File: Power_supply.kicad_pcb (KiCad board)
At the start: 2 copper layers, 160 x 40 mm, 49 parts, among them J20 HV_Transformer, J21 LV_Transformer, J22 220V, J23 Transformers, J24 Thyratrone, J25 Anodes_enable, J26 Conn_01x04, J27 Conn_01x04, J28 Conn_01x04, K2 SANYOU_SRD_Form_C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

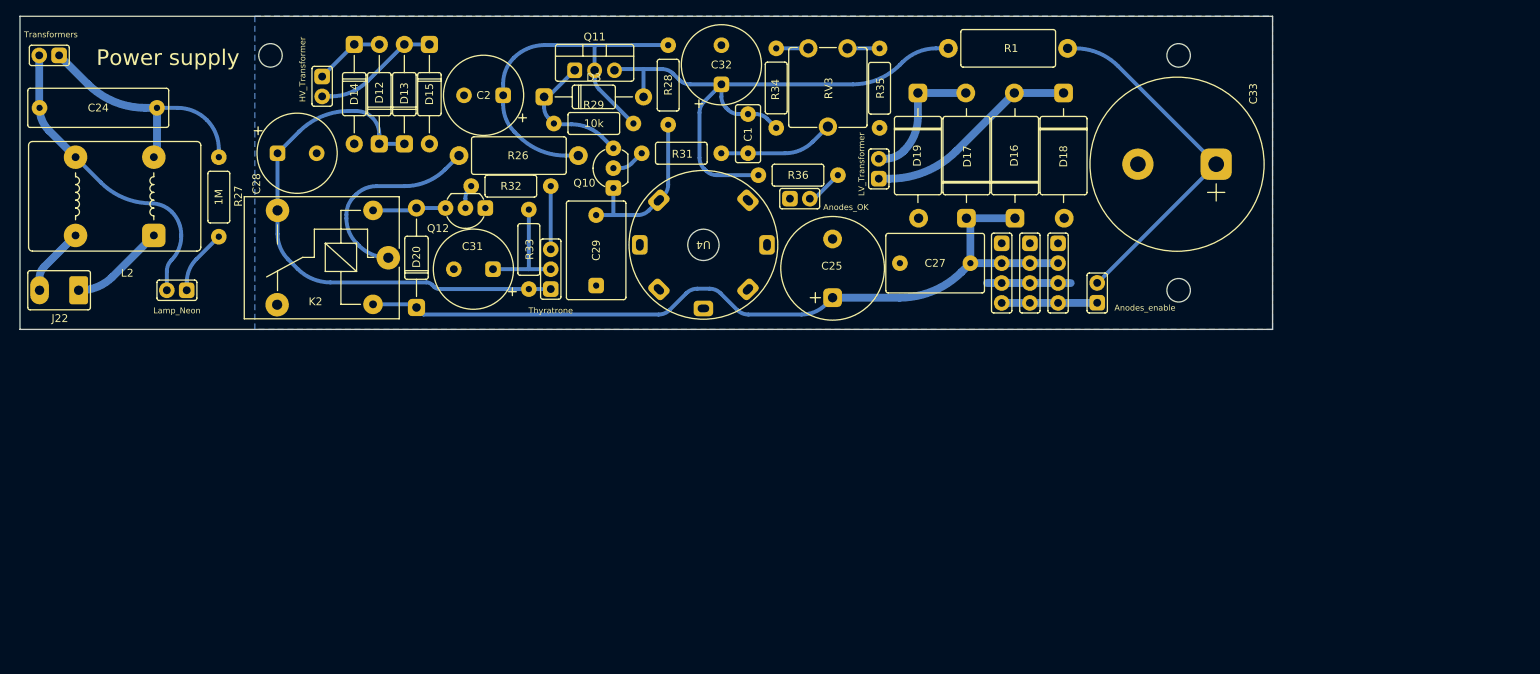
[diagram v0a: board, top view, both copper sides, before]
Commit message: New power supply PCB
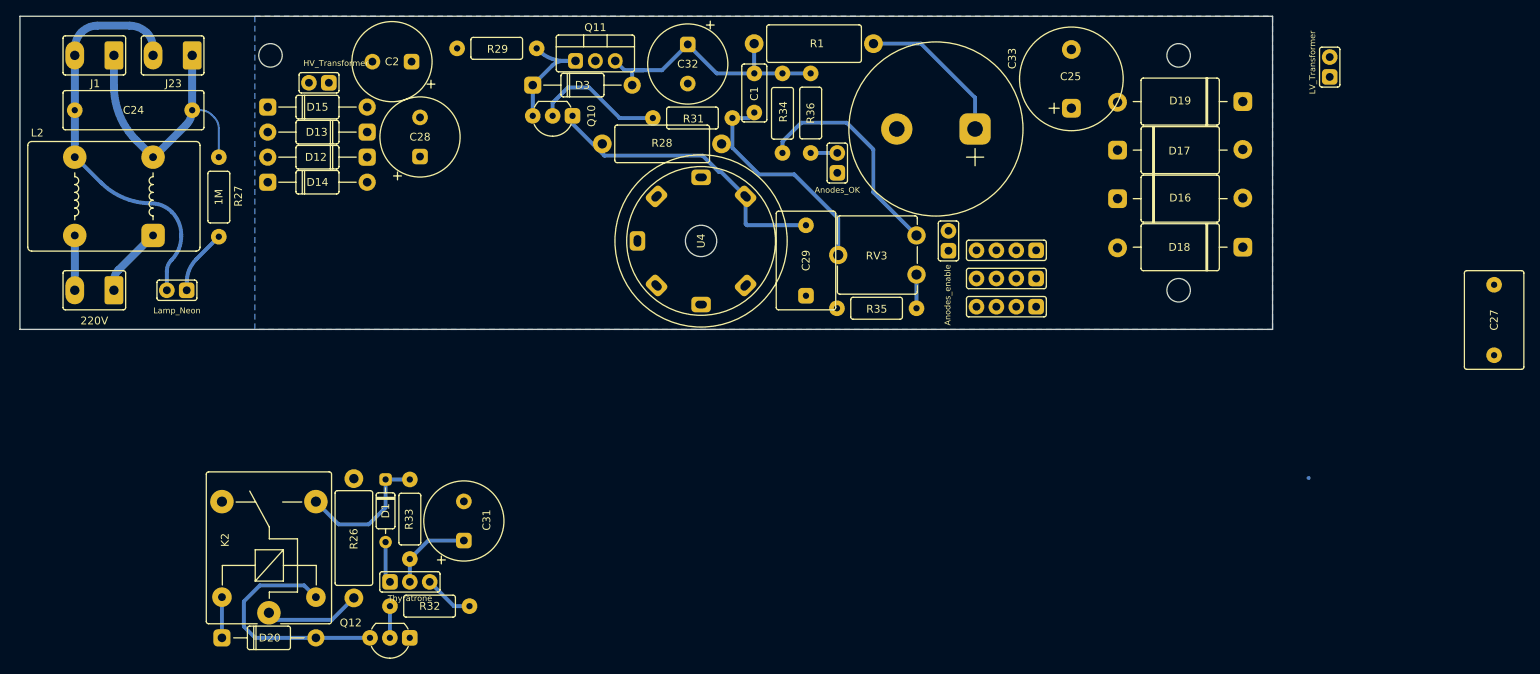
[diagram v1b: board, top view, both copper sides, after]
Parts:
- added D1: BZX55C75, spdf1626_lib:D_THT_DO-35_SOD27_Horizontal, F.Cu at (76.7, 153.2)
- added J1: Transformers, spdf1626_lib:Connector_1x02_P5mm_Vertical, F.Cu at (39.5, 95.0)
- J23: footprint spdf1626_lib:PinHeader_1x02_P2.54mm -> spdf1626_lib:Connector_1x02_P5mm_Vertical
- K2: footprint Relay_THT:Relay_SPDT_SANYOU_SRD_Series_Form_C -> spdf1626_lib:Relay_THT_SRD_Series
- R28: footprint spdf1626_lib:R_THT_025W -> spdf1626_lib:R_THT_1W
- moved C27 71.8 mm to (218.3, 128.8), turned to 90 degrees
- moved J21 59.0 mm to (197.3, 97.7)
- moved R26 58.1 mm to (72.7, 164.3), turned to 90 degrees
- moved Q12 55.7 mm to (77.2, 169.4)
- moved R32 54.6 mm to (87.4, 165.3)
- moved K2 47.8 mm to (61.8, 166.2), turned to 90 degrees
- moved R33 47.2 mm to (79.8, 159.3), turned to 90 degrees
- moved D20 46.2 mm to (61.8, 169.4), turned to 0 degrees
- moved J24 42.7 mm to (77.3, 162.2), turned to 90 degrees
- moved C25 38.9 mm to (164.3, 101.8)
- moved C31 34.9 mm to (86.7, 157.0), turned to 90 degrees
- moved D19 34.2 mm to (178.2, 100.9), turned to 180 degrees
- moved R35 33.5 mm to (144.5, 127.3), turned to 180 degrees
- moved C33 31.1 mm to (152.0, 104.4)
- moved RV3 27.6 mm to (144.5, 118.0), turned to 180 degrees
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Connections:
- J24 pad 1: HV -> Net-(J24-Pad1)
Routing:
- net +6V: track 104.5 -> 5.20 mm
- net Net-(C2-Pad1): track 55.2 -> 0.00 mm
- net HV: track 69.4 -> 17.7 mm
- net Net-(C1-Pad2): track 77.7 -> 35.5 mm
- net Net-(D16-Pad2): track 27.6 -> 0.00 mm
- net Net-(C33-Pad1): track 46.2 -> 19.9 mm
- net Net-(R34-Pad2): track 4.10 -> 28.7 mm
- net Net-(D20-Pad2): track 9.38 -> 30.6 mm
- net Net-(D17-Pad2): track 17.4 -> 0.00 mm
- net Net-(D13-Pad2): track 16.1 -> 0.00 mm
- net Net-(Q10-Pad1): track 22.2 -> 38.3 mm
- net Net-(C1-Pad1): track 14.8 -> 28.8 mm
- net K1.1: track 26.1 -> 12.4 mm
- net Net-(C24-Pad1): track 40.1 -> 53.4 mm
- net Net-(Q10-Pad2): track 4.31 -> 16.9 mm
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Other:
- board text removed: "Power supply"

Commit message: Working on power supply PCB
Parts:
- moved Q12 53.0 mm to (80.0, 116.5)
- moved J24 50.8 mm to (88.4, 112.7), turned to 0 degrees
- moved R33 50.4 mm to (87.7, 109.5), turned to 180 degrees
- moved R26 50.0 mm to (103.2, 124.7)
- moved R32 44.7 mm to (87.8, 120.7)
- moved D20 44.1 mm to (68.1, 125.8)
- moved K2 44.1 mm to (68.1, 122.6)
- moved C31 42.0 mm to (95.0, 115.8), turned to -90 degrees
- moved D1 40.8 mm to (81.5, 112.7), turned to 0 degrees
- moved C2 17.7 mm to (95.0, 105.3), turned to -90 degrees
- moved R29 12.6 mm to (108.4, 92.0)
- moved D15 10.7 mm to (68.0, 93.0)
- moved D13 10.7 mm to (80.8, 96.2)
- moved D12 10.7 mm to (80.8, 99.4)
- moved D14 10.7 mm to (68.0, 102.6)
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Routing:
- net +6V: track 5.20 -> 75.0 mm
- net K1.1: track 12.4 -> 36.0 mm
- net HV: track 17.7 -> 28.3 mm
- net Net-(C31-Pad1): track 10.8 -> 15.6 mm
- net Net-(J24-Pad3): track 6.36 -> 3.17 mm
- net Net-(J24-Pad1): track 5.33 -> 2.90 mm
- net Net-(Q12-Pad2): track 4.05 -> 5.18 mm
- net Net-(D20-Pad2): track 30.6 -> 30.0 mm

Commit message: Working on power supply PCB
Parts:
- moved R28 30.5 mm to (133.5, 97.2), turned to -90 degrees
- moved R29 20.2 mm to (89.0, 97.6), turned to 0 degrees
- moved Q10 18.7 mm to (116.7, 100.9), turned to 90 degrees
- moved R33 13.6 mm to (85.8, 123.0), turned to 90 degrees
- moved R1 11.3 mm to (112.6, 95.0)
- moved C32 9.79 mm to (109.4, 101.4)
- moved D20 9.27 mm to (61.8, 119.0), turned to 90 degrees
- moved Q11 8.00 mm to (99.2, 102.5)
- moved R31 6.56 mm to (123.7, 109.0), turned to 90 degrees
- moved D1 6.28 mm to (87.3, 110.3)
- moved C2 4.49 mm to (99.2, 106.9)
- moved K2 4.16 mm to (71.5, 125.0)
- moved J24 3.98 mm to (91.8, 114.8)
- moved D3 3.97 mm to (96.7, 95.0)
- moved C31 3.81 mm to (98.5, 117.3)
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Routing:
- net Net-(Q10-Pad1): track 38.3 -> 0.00 mm
- net Net-(R34-Pad2): track 28.7 -> 0.00 mm
- net Net-(D3-Pad1): track 16.0 -> 42.8 mm
- net Net-(C1-Pad1): track 28.8 -> 6.45 mm
- net Net-(C1-Pad2): track 35.5 -> 17.7 mm
- net Net-(C2-Pad1): track 0.00 -> 17.7 mm
- net Net-(D13-Pad2): track 0.00 -> 10.2 mm
- net Net-(Q10-Pad2): track 16.9 -> 7.86 mm
- net Net-(D20-Pad2): track 30.0 -> 25.0 mm
- net Net-(Q12-Pad2): track 5.18 -> 10.1 mm
- net HV: track 28.3 -> 31.1 mm
- net Net-(J24-Pad1): track 2.90 -> 4.67 mm
- net K1.1: track 36.0 -> 34.3 mm
- net Net-(J24-Pad3): track 3.17 -> 4.43 mm
- net Net-(C31-Pad1): track 15.6 -> 16.9 mm

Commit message: New power supply PCB!
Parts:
- moved C27 53.4 mm to (165.0, 125.4), turned to 180 degrees
- moved R29 39.6 mm to (125.8, 112.3), turned to 90 degrees
- moved R28 39.4 mm to (94.9, 104.9), turned to 0 degrees
- moved R35 38.8 mm to (165.8, 94.8), turned to -90 degrees
- moved R1 34.3 mm to (146.9, 94.8), turned to -90 degrees
- moved J21 29.2 mm to (185.8, 124.6), turned to -90 degrees
- moved D3 20.7 mm to (113.9, 106.4), turned to 90 degrees
- moved Q11 20.2 mm to (119.2, 99.5), turned to 90 degrees
- moved NE4 19.8 mm to (153.5, 104.7), turned to -90 degrees
- moved RV3 19.4 mm to (151.1, 99.8), turned to 0 degrees
- moved C32 18.7 mm to (127.9, 98.7), turned to 90 degrees
- moved C31 18.6 mm to (96.5, 98.8), turned to 90 degrees
- moved C33 17.5 mm to (142.1, 118.8)
- moved R32 16.1 mm to (81.1, 108.8), turned to -90 degrees
- moved C25 14.4 mm to (161.6, 115.9)
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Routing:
- net +6V: track 75.0 -> 143.5 mm
- net Net-(C1-Pad1): track 6.45 -> 46.6 mm
- net Net-(C2-Pad1): track 17.7 -> 51.4 mm
- net Net-(D17-Pad2): track 0.00 -> 26.1 mm
- net Net-(C29-Pad2): track 0.00 -> 24.6 mm
- net Net-(C1-Pad2): track 17.7 -> 40.3 mm
- net Net-(D3-Pad1): track 42.8 -> 21.1 mm
- net Net-(NE4-Pad2): track 3.40 -> 17.6 mm
- net 240V: track 0.00 -> 13.7 mm
- net Net-(D16-Pad2): track 0.00 -> 11.6 mm
- net Net-(R34-Pad2): track 0.00 -> 11.5 mm
- net Net-(R35-Pad1): track 4.30 -> 14.7 mm
- net K1.1: track 34.3 -> 24.3 mm
- net GND: track 0.00 -> 8.86 mm
- net HV: track 31.1 -> 38.9 mm
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
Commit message: Power supply PCB final 1.0
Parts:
- turned U4 to 0 degrees
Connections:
- U4 pad 1: Net-(C29-Pad2) -> unconnected-(U4-Pad1)
- U4 pad 4: unconnected-(U4-Pad4) -> GND
- U4 pad 5: unconnected-(U4-Pad5) -> Net-(C29-Pad2)
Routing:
- net Net-(C29-Pad2): track 24.6 -> 35.1 mm
- net +6V: track 143.5 -> 140.5 mm
- net Net-(C1-Pad1): track 46.6 -> 45.4 mm

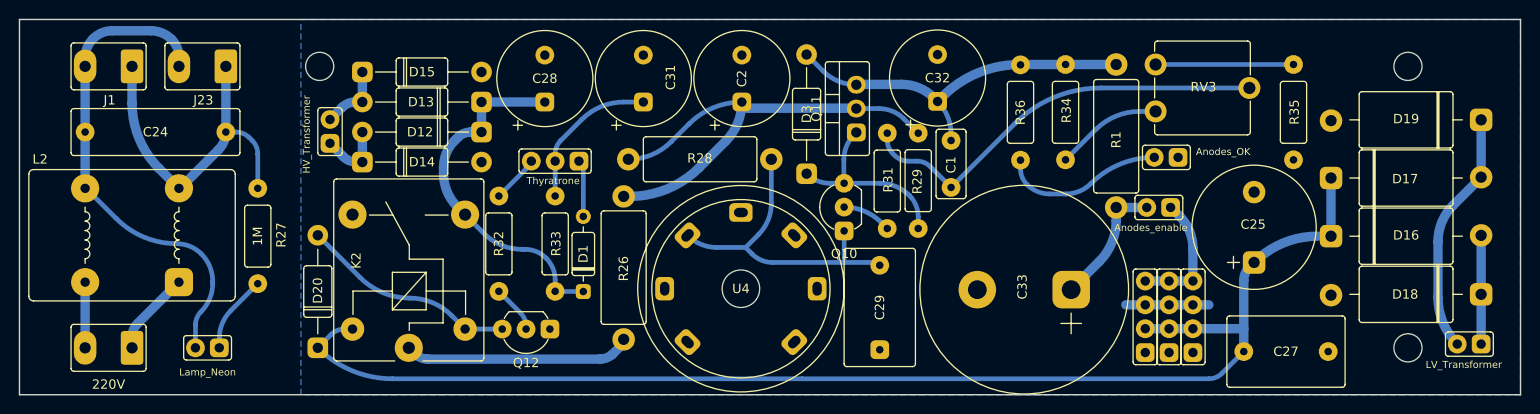
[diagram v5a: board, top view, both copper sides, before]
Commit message: Some errors in the power supply PCB fixed
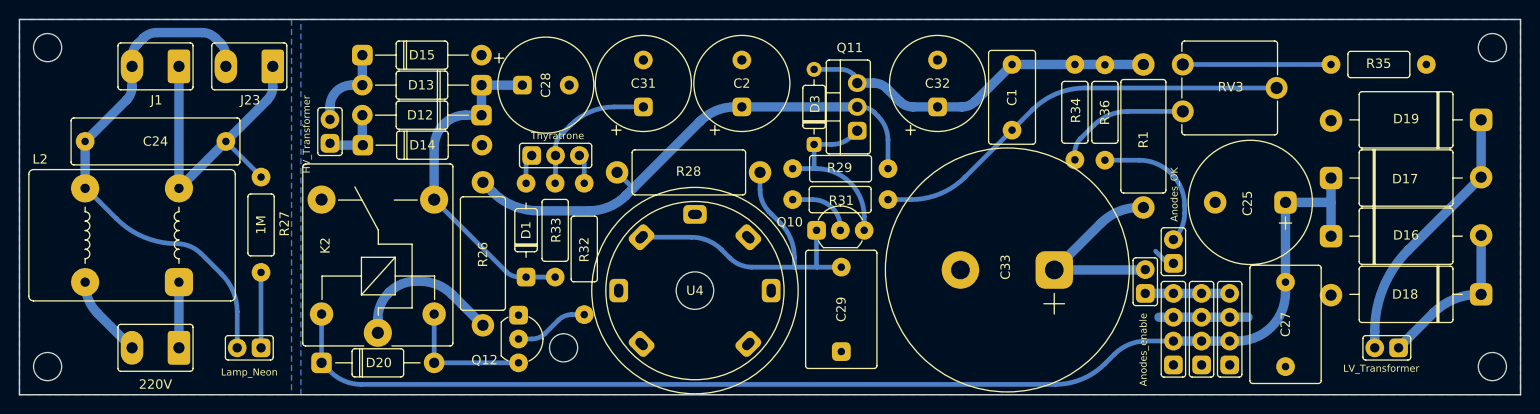
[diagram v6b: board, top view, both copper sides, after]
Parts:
- C1: footprint spdf1626_lib:C_THT_K73-17_P5.00mm -> spdf1626_lib:C_THT_K73-17_P7.00mm
- D3: footprint spdf1626_lib:D_DO-41 -> spdf1626_lib:D_THT_DO-35_SOD27_Horizontal
- moved R26 15.1 mm to (79.4, 122.6)
- moved R29 14.8 mm to (112.4, 105.9), turned to 0 degrees
- moved C1 11.6 mm to (135.8, 98.3)
- moved NE4 11.3 mm to (153.0, 116.0), turned to 180 degrees
- moved R32 10.7 mm to (90.2, 114.5)
- moved D20 9.94 mm to (68.2, 126.6), turned to 0 degrees
- moved J25 9.55 mm to (150.0, 119.2), turned to 180 degrees
- moved R36 9.00 mm to (145.7, 105.0)
- moved J21 8.81 mm to (177.0, 125.0)
- moved C25 7.22 mm to (164.9, 109.5), turned to 180 degrees
- moved D3 7.16 mm to (114.7, 99.3)
- moved C33 7.12 mm to (135.3, 116.7)
- moved R31 7.08 mm to (122.6, 109.2), turned to 180 degrees
- moved D1 6.61 mm to (84.0, 112.5)
- moved J24 5.08 mm to (84.6, 104.5), turned to 90 degrees
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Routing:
- net Net-(D20-Pad2): track 23.0 -> 14.2 mm
- net Net-(C33-Pad1): track 13.8 -> 21.7 mm
- net K1.1: track 24.3 -> 16.6 mm
- net +6V: track 140.5 -> 134.0 mm
- net Net-(D16-Pad2): track 11.6 -> 17.1 mm
- net 240V: track 13.7 -> 9.00 mm
- net Net-(C2-Pad1): track 51.4 -> 55.7 mm
- net HV: track 38.9 -> 35.7 mm
- net GND: track 8.86 -> 11.9 mm
- net Net-(D1-Pad2): track 6.09 -> 3.21 mm
- net Net-(Q12-Pad2): track 5.03 -> 7.88 mm
- net Net-(R34-Pad2): track 11.5 -> 14.3 mm
- net Net-(NE4-Pad2): track 17.6 -> 15.0 mm
- net Net-(C24-Pad2): track 37.8 -> 35.4 mm
- net Net-(D17-Pad2): track 26.1 -> 28.4 mm
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- added copper zone on B.Cu, net (none)
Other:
- outline, holes or cut-outs redrawn

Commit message: Added heatsink on power mosfet
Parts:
- moved R31 9.73 mm to (128.9, 101.8), turned to -135 degrees
- moved R36 8.20 mm to (153.9, 105.0)
- moved C1 5.60 mm to (141.4, 98.3)
- moved C32 5.54 mm to (133.4, 96.8)
- moved Q11 3.35 mm to (122.7, 99.3)
- moved RV3 3.30 mm to (157.3, 99.8)
- moved R34 3.20 mm to (145.7, 94.8)
- moved D3 2.90 mm to (117.6, 99.3)
- moved Q10 2.68 mm to (117.6, 109.8), turned to 90 degrees
- moved R29 2.56 mm to (114.5, 104.4), turned to 90 degrees
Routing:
- net Net-(C29-Pad2): track 37.4 -> 30.3 mm
- net Net-(D3-Pad1): track 19.4 -> 12.9 mm
- net Net-(NE4-Pad2): track 15.0 -> 8.76 mm
- net Net-(C1-Pad1): track 45.6 -> 39.7 mm
- net Net-(R35-Pad1): track 15.8 -> 12.5 mm
- net Net-(Q10-Pad2): track 6.97 -> 4.35 mm
- net Net-(C1-Pad2): track 38.0 -> 39.1 mm
- net Net-(R34-Pad2): track 14.3 -> 13.3 mm
